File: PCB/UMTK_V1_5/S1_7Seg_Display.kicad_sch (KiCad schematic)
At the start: 7 parts, among them U10 CA56-12EWA, U2 SN74LVC1T45DCK, U3 SN74LVC1T45DCK, U7 MAX7221xWG, U8 SN74LVC1T45DCK, U9 CA56-12EWA

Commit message: Schematic Done, Assigning footprint
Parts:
- renumbered R1 to R33, U2 to U3, U3 to U4, U8 to U5, U7 to U6, U10 to U7, U9 to U8
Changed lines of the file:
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@@
 		(on_board yes)
 		(dnp no)
-		(property "Reference" "#PWR09"
+		(property "Reference" "#PWR044"
 			(at 51.816 186.69 0)
 			(effects
@@
 			(project "UMTK"
 				(path "/2bf3ea67-58b8-47b3-a768-ea6950b40edf/96966801-b9b1-4005-b7bb-fead645709bc"
-					(reference "#PWR09")
+					(reference "#PWR044")
 					(unit 1)
 				)
@@
 		(dnp no)
 		(fields_autoplaced yes)
-		(property "Reference" "U2"
+		(property "Reference" "U3"
 			(at 58.42 71.1514 0)
 			(effects
@@
 			(project ""
 				(path "/2bf3ea67-58b8-47b3-a768-ea6950b40edf/96966801-b9b1-4005-b7bb-fead645709bc"
-					(reference "U2")
+					(reference "U3")
 					(unit 1)
 				)
@@
 		(dnp no)
 		(fields_autoplaced yes)
-		(property "Reference" "#PWR08"
+		(property "Reference" "#PWR041"
 			(at 38.1 158.75 0)
 			(effects
@@
 			(project "UMTK"
 				(path "/2bf3ea67-58b8-47b3-a768-ea6950b40edf/96966801-b9b1-4005-b7bb-fead645709bc"
-					(reference "#PWR08")
+					(reference "#PWR041")
 					(unit 1)
 				)
@@
 		(dnp no)
 		(fields_autoplaced yes)
-		(property "Reference" "R1"
+		(property "Reference" "R33"
 			(at 96.52 86.3599 0)
 			(effects
@@
 			(project ""
 				(path "/2bf3ea67-58b8-47b3-a768-ea6950b40edf/96966801-b9b1-4005-b7bb-fead645709bc"
-					(reference "R1")
+					(reference "R33")
 					(unit 1)
 				)
@@
 		(on_board yes)
 		(dnp no)
-		(property "Reference" "#PWR06"
+		(property "Reference" "#PWR043"
 			(at 51.816 139.7 0)
 			(effects
@@
 			(project "UMTK"
 				(path "/2bf3ea67-58b8-47b3-a768-ea6950b40edf/96966801-b9b1-4005-b7bb-fead645709bc"
-					(reference "#PWR06")
+					(reference "#PWR043")
 					(unit 1)
 				)
@@
 		(on_board yes)
 		(dnp no)
-		(property "Reference" "#PWR04"
+		(property "Reference" "#PWR042"
 			(at 51.816 93.98 0)
 			(effects
@@
 			(project ""
 				(path "/2bf3ea67-58b8-47b3-a768-ea6950b40edf/96966801-b9b1-4005-b7bb-fead645709bc"
-					(reference "#PWR04")
+					(reference "#PWR042")
 					(unit 1)
 				)
@@
 		(dnp no)
 		(fields_autoplaced yes)
-		(property "Reference" "U7"
+		(property "Reference" "U6"
 			(at 111.4141 87.63 0)
 			(effects
@@
 			(project ""
 				(path "/2bf3ea67-58b8-47b3-a768-ea6950b40edf/96966801-b9b1-4005-b7bb-fead645709bc"
-					(reference "U7")
+					(reference "U6")
 					(unit 1)
 				)
@@
 		(dnp no)
 		(fields_autoplaced yes)
-		(property "Reference" "#PWR010"
+		(property "Reference" "#PWR047"
 			(at 43.18 158.75 0)
 			(effects
@@
 			(project "UMTK"
 				(path "/2bf3ea67-58b8-47b3-a768-ea6950b40edf/96966801-b9b1-4005-b7bb-fead645709bc"
-					(reference "#PWR010")
+					(reference "#PWR047")
 					(unit 1)
 				)
@@
 		(dnp no)
 		(fields_autoplaced yes)
-		(property "Reference" "#PWR013"
+		(property "Reference" "#PWR038"
 			(at 15.24 173.99 0)
 			(effects
@@
 			(project "UMTK"
 				(path "/2bf3ea67-58b8-47b3-a768-ea6950b40edf/96966801-b9b1-4005-b7bb-fead645709bc"
-					(reference "#PWR013")
+					(reference "#PWR038")
 					(unit 1)
 				)
@@
 		(dnp no)
 		(fields_autoplaced yes)
-		(property "Reference" "#PWR03"
+		(property "Reference" "#PWR048"
 			(at 109.22 86.36 0)
 			(effects
@@
 			(project "UMTK"
 				(path "/2bf3ea67-58b8-47b3-a768-ea6950b40edf/96966801-b9b1-4005-b7bb-fead645709bc"
-					(reference "#PWR03")
+					(reference "#PWR048")
 					(unit 1)
 				)
@@
 		(dnp no)
 		(fields_autoplaced yes)
-		(property "Reference" "U10"
+		(property "Reference" "U7"
 			(at 201.93 160.02 0)
 			(effects
@@
 			(project "UMTK"
 				(path "/2bf3ea67-58b8-47b3-a768-ea6950b40edf/96966801-b9b1-4005-b7bb-fead645709bc"
-					(reference "U10")
+					(reference "U7")
 					(unit 1)
 				)
@@
 		(dnp no)
 		(fields_autoplaced yes)
-		(property "Reference" "U9"
+		(property "Reference" "U8"
 			(at 203.2 71.12 0)
 			(effects
@@
 			(project ""
 				(path "/2bf3ea67-58b8-47b3-a768-ea6950b40edf/96966801-b9b1-4005-b7bb-fead645709bc"
-					(reference "U9")
+					(reference "U8")
 					(unit 1)
 				)
@@
 		(dnp no)
 		(fields_autoplaced yes)
-		(property "Reference" "U8"
+		(property "Reference" "U5"
 			(at 58.42 163.8614 0)
 			(effects
@@
 			(project "UMTK"
 				(path "/2bf3ea67-58b8-47b3-a768-ea6950b40edf/96966801-b9b1-4005-b7bb-fead645709bc"
-					(reference "U8")
+					(reference "U5")
 					(unit 1)
 				)
@@
 		(on_board yes)
 		(dnp no)
-		(property "Reference" "#PWR07"
+		(property "Reference" "#PWR046"
 			(at 43.18 111.76 0)
 			(effects
@@
 			(project "UMTK"
 				(path "/2bf3ea67-58b8-47b3-a768-ea6950b40edf/96966801-b9b1-4005-b7bb-fead645709bc"
-					(reference "#PWR07")
+					(reference "#PWR046")
 					(unit 1)
 				)
@@
 		(on_board yes)
 		(dnp no)
-		(property "Reference" "#PWR05"
+		(property "Reference" "#PWR040"
 			(at 38.1 111.76 0)
 			(effects
@@
 			(project "UMTK"
 				(path "/2bf3ea67-58b8-47b3-a768-ea6950b40edf/96966801-b9b1-4005-b7bb-fead645709bc"
-					(reference "#PWR05")
+					(reference "#PWR040")
 					(unit 1)
 				)
@@
 		(dnp no)
 		(fields_autoplaced yes)
-		(property "Reference" "#PWR011"
+		(property "Reference" "#PWR036"
 			(at 15.24 81.28 0)
 			(effects
@@
 			(project "UMTK"
 				(path "/2bf3ea67-58b8-47b3-a768-ea6950b40edf/96966801-b9b1-4005-b7bb-fead645709bc"
-					(reference "#PWR011")
+					(reference "#PWR036")
 					(unit 1)
 				)
@@
 		(dnp no)
 		(fields_autoplaced yes)
-		(property "Reference" "#PWR012"
+		(property "Reference" "#PWR037"
 			(at 15.24 127 0)
 			(effects
@@
 			(project "UMTK"
 				(path "/2bf3ea67-58b8-47b3-a768-ea6950b40edf/96966801-b9b1-4005-b7bb-fead645709bc"
-					(reference "#PWR012")
+					(reference "#PWR037")
 					(unit 1)
 				)
@@
 		(dnp no)
 		(fields_autoplaced yes)
-		(property "Reference" "#PWR01"
+		(property "Reference" "#PWR039"
 			(at 38.1 66.04 0)
 			(effects
@@
 			(project ""
 				(path "/2bf3ea67-58b8-47b3-a768-ea6950b40edf/96966801-b9b1-4005-b7bb-fead645709bc"
-					(reference "#PWR01")
+					(reference "#PWR039")
 					(unit 1)
 				)
@@
 		(on_board yes)
 		(dnp no)
-		(property "Reference" "#PWR014"
+		(property "Reference" "#PWR049"
 			(at 120.396 146.05 0)
 			(effects
@@
 			(project "UMTK"
 				(path "/2bf3ea67-58b8-47b3-a768-ea6950b40edf/96966801-b9b1-4005-b7bb-fead645709bc"
-					(reference "#PWR014")
+					(reference "#PWR049")
 					(unit 1)
 				)
@@
 		(dnp no)
 		(fields_autoplaced yes)
-		(property "Reference" "#PWR02"
+		(property "Reference" "#PWR045"
 			(at 43.18 66.04 0)
 			(effects
@@
 			(project ""
 				(path "/2bf3ea67-58b8-47b3-a768-ea6950b40edf/96966801-b9b1-4005-b7bb-fead645709bc"
-					(reference "#PWR02")
+					(reference "#PWR045")
 					(unit 1)
 				)
@@
 		(dnp no)
 		(fields_autoplaced yes)
-		(property "Reference" "U3"
+		(property "Reference" "U4"
 			(at 58.42 116.8714 0)
 			(effects
@@
 			(project "UMTK"
 				(path "/2bf3ea67-58b8-47b3-a768-ea6950b40edf/96966801-b9b1-4005-b7bb-fead645709bc"
-					(reference "U3")
-					(unit 1)
-				)
+					(reference "U4")
+					(unit 1)
+				)

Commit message: Footprint assign
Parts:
- R33: value 9k53 -> 10k; footprint (none) -> Resistor_SMD:R_0402_1005Metric
- U3, U4, U5: footprint Package_TO_SOT_SMD:SOT-363_SC-70-6 -> Package_TO_SOT_SMD:SOT-23-6
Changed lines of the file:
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@@
 			)
 		)
-		(property "Footprint" "Package_TO_SOT_SMD:SOT-363_SC-70-6"
+		(property "Footprint" "Package_TO_SOT_SMD:SOT-23-6"
 			(at 40.64 88.9 0)
 			(effects
@@
 			)
 		)
-		(property "Value" "9k53"
+		(property "Value" "10k"
 			(at 96.52 88.8999 0)
 			(effects
@@
 			)
 		)
-		(property "Footprint" ""
+		(property "Footprint" "Resistor_SMD:R_0402_1005Metric"
 			(at 94.996 87.884 90)
 			(effects
@@
 			)
 		)
-		(property "Footprint" "Package_TO_SOT_SMD:SOT-363_SC-70-6"
+		(property "Footprint" "Package_TO_SOT_SMD:SOT-23-6"
 			(at 40.64 181.61 0)
 			(effects
@@
 			)
 		)
-		(property "Footprint" "Package_TO_SOT_SMD:SOT-363_SC-70-6"
+		(property "Footprint" "Package_TO_SOT_SMD:SOT-23-6"
 			(at 40.64 134.62 0)
 			(effects

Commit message: ERC good, imported into PCB
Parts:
- U3, U4, U5: footprint Package_TO_SOT_SMD:SOT-23-6 -> Package_TO_SOT_SMD:SOT-363_SC-70-6
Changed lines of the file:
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@@
 			)
 		)
-		(property "Footprint" "Package_TO_SOT_SMD:SOT-23-6"
+		(property "Footprint" "Package_TO_SOT_SMD:SOT-363_SC-70-6"
 			(at 40.64 88.9 0)
 			(effects
@@
 			)
 		)
-		(property "Footprint" "Package_TO_SOT_SMD:SOT-23-6"
+		(property "Footprint" "Package_TO_SOT_SMD:SOT-363_SC-70-6"
 			(at 40.64 181.61 0)
 			(effects
@@
 			)
 		)
-		(property "Footprint" "Package_TO_SOT_SMD:SOT-23-6"
+		(property "Footprint" "Package_TO_SOT_SMD:SOT-363_SC-70-6"
 			(at 40.64 134.62 0)
 			(effects

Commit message: Make simple components bigger
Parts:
- R33: footprint Resistor_SMD:R_0402_1005Metric -> Resistor_SMD:R_0603_1608Metric
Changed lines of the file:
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@@
 			)
 		)
-		(property "Footprint" "Resistor_SMD:R_0402_1005Metric"
+		(property "Footprint" "Resistor_SMD:R_0603_1608Metric"
 			(at 94.996 87.884 90)
 			(effects

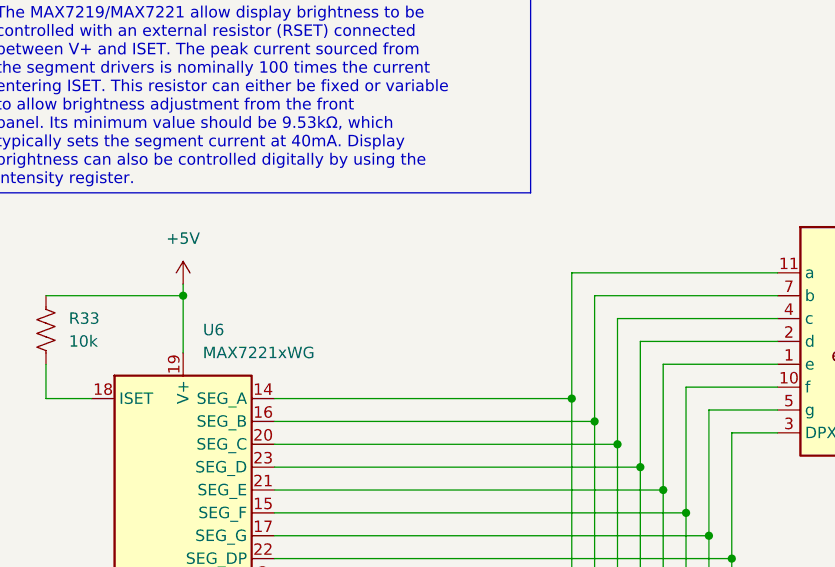
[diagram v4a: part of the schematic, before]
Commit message: Add a bit of decoupling for 7seg driver
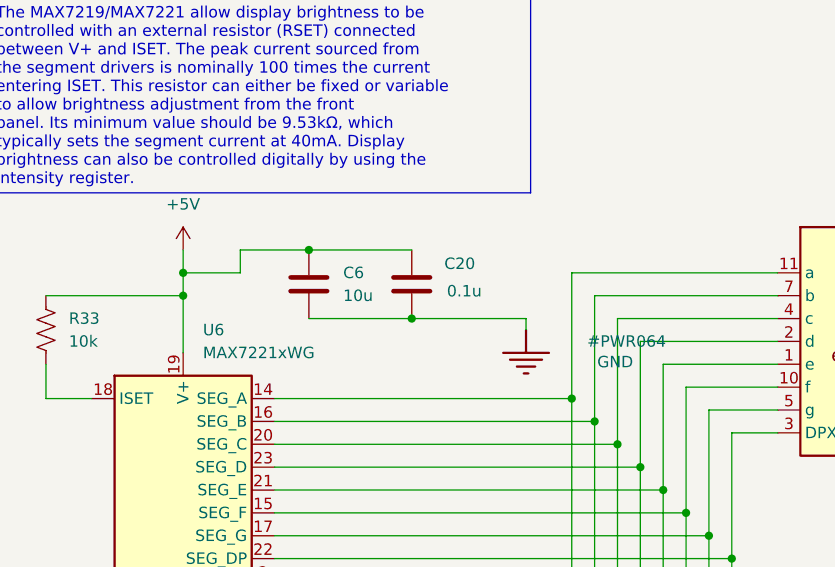
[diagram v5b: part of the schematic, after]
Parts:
- added C20: 0.1u, Capacitor_SMD:C_0603_1608Metric, symbol Device:C
- added C6: 10u, Capacitor_SMD:C_0805_2012Metric, symbol Device:C
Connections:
- net +5V: now also C20.2, C6.2
- net GND: now also C20.1, C6.1

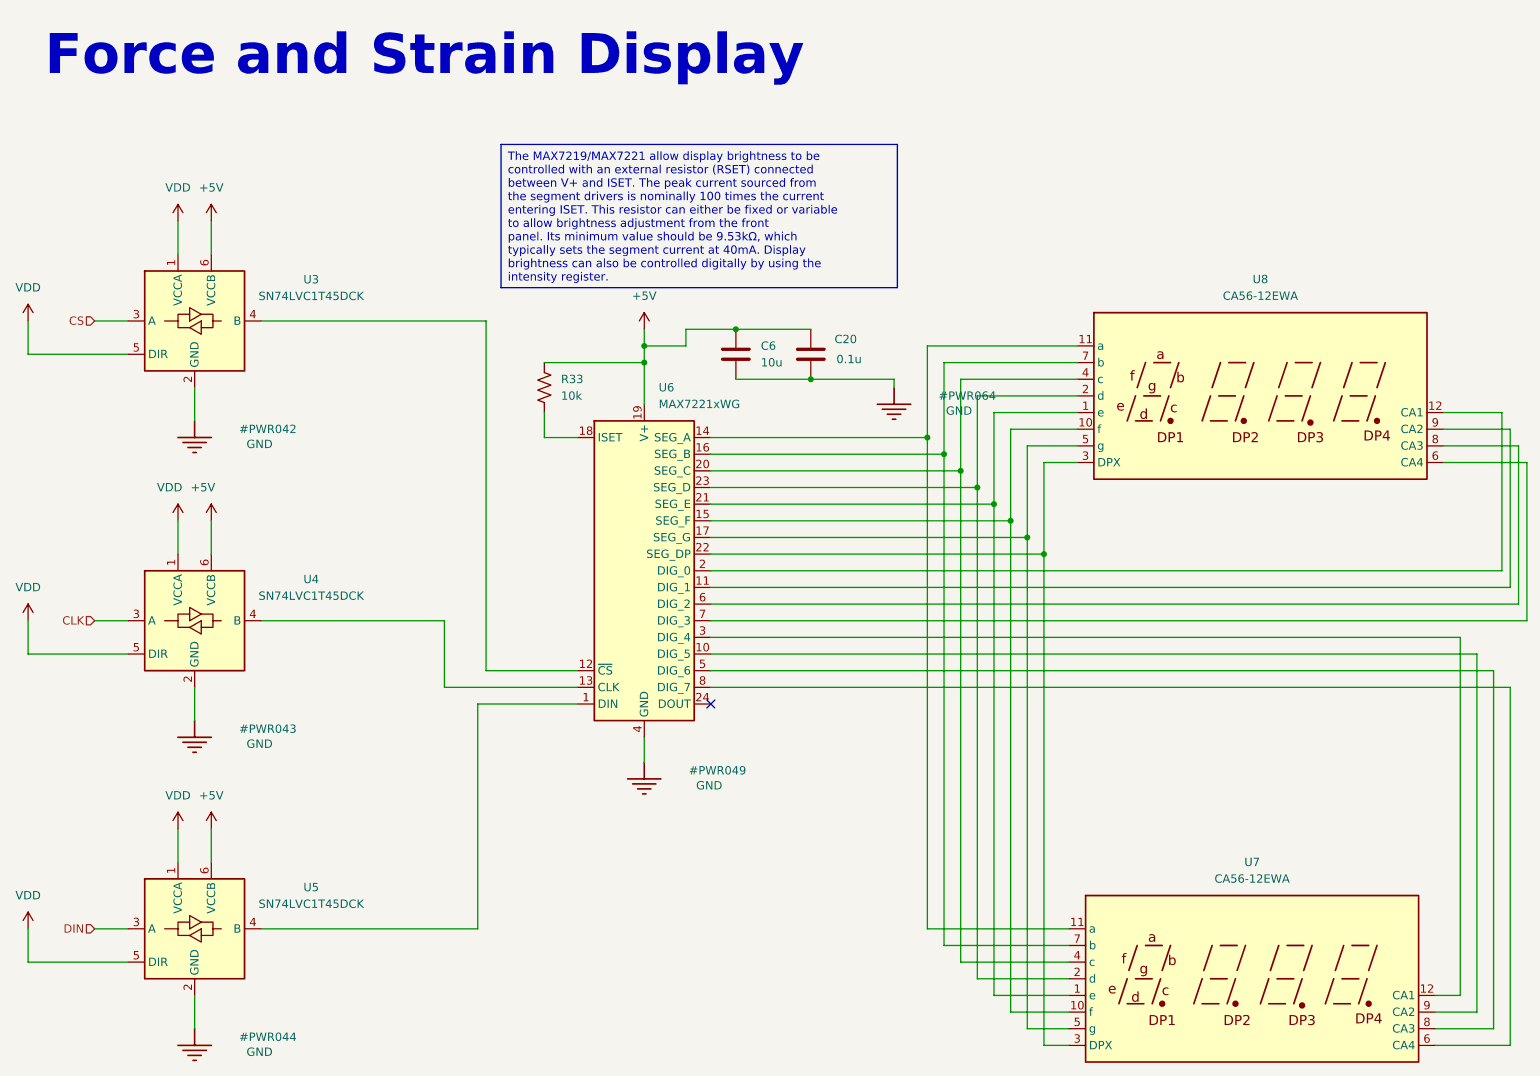
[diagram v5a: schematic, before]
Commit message: PCB Revision
- Add filter for 7seg power again
- Add low pass filter for output of motor power sense
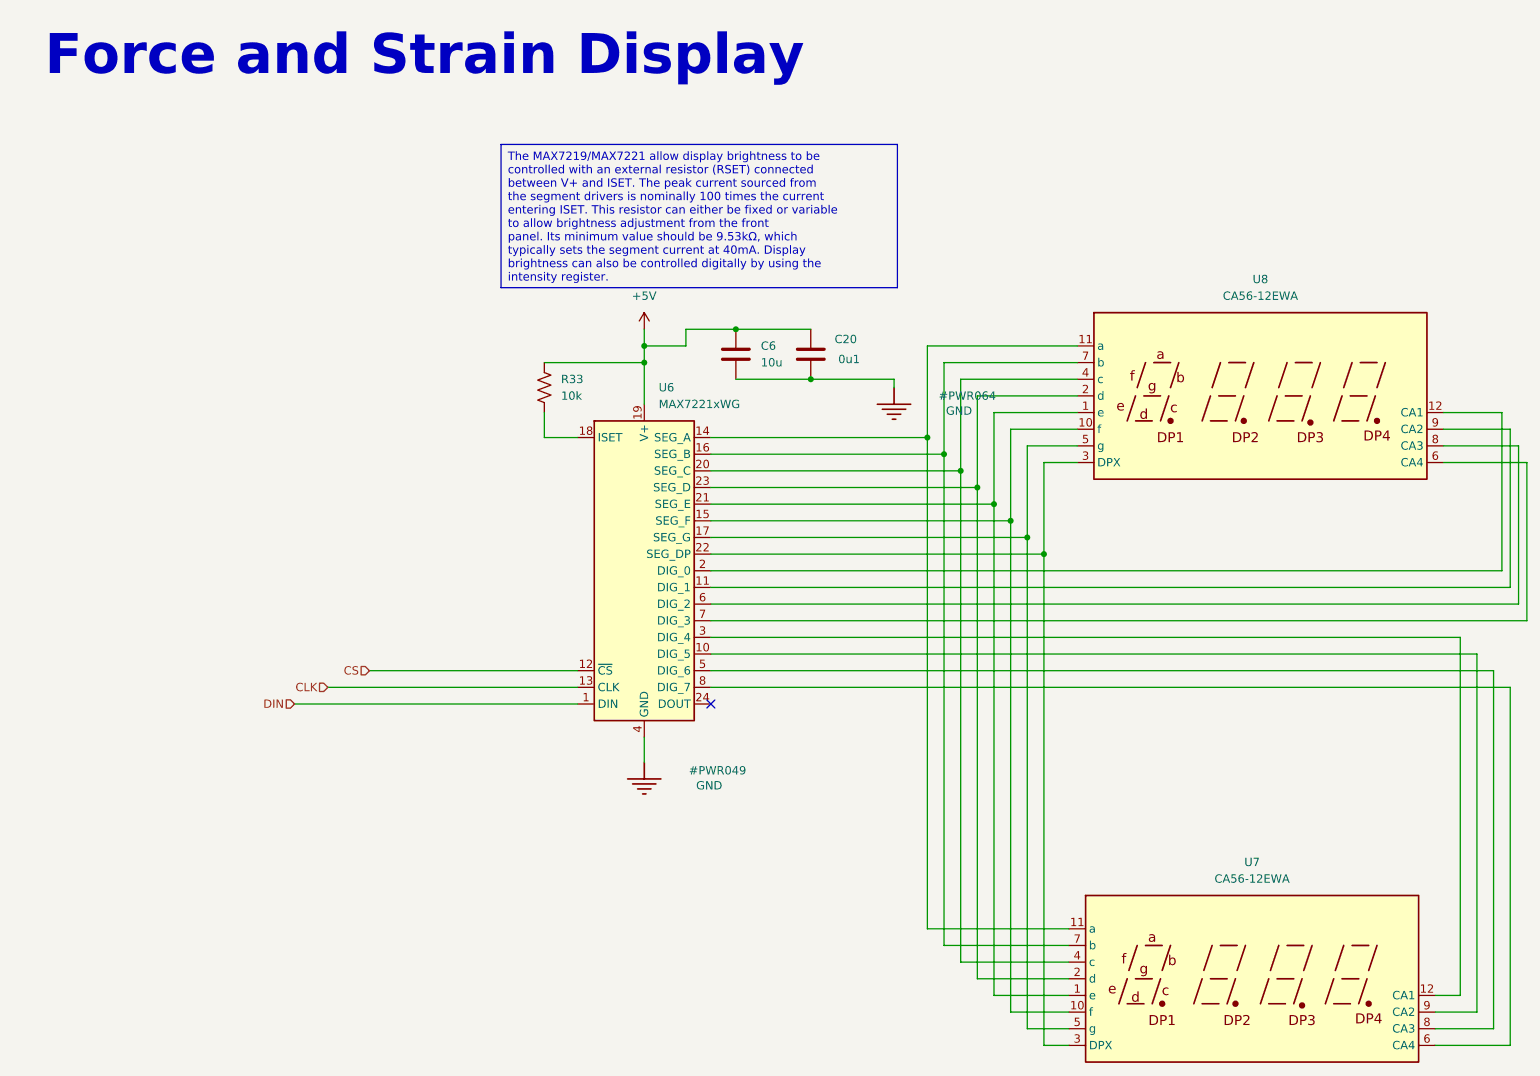
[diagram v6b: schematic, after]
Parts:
- removed U3, U4, U5: SN74LVC1T45DCK, Package_TO_SOT_SMD:SOT-363_SC-70-6, symbol Logic_LevelTranslator:SN74LVC1T45DCK
- C20: value 0.1u -> 0u1
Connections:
- net CLK: now also U6.13 (CLK)
- net CS: now also U6.12 (~{CS})
- net DIN: now also U6.1 (DIN)
